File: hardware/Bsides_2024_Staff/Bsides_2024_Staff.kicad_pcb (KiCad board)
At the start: 2 copper layers, 129.4 x 129.4 mm, 59 parts, among them J1 Serial_IN, J2 Add_On, J3 OLED, J4 Serial_OUT, J5 Battery, J6 Battery, P1 USB_C_Plug_USB2.0, Q1 DMG3415U-7, SW1 ON, SW2 RESET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

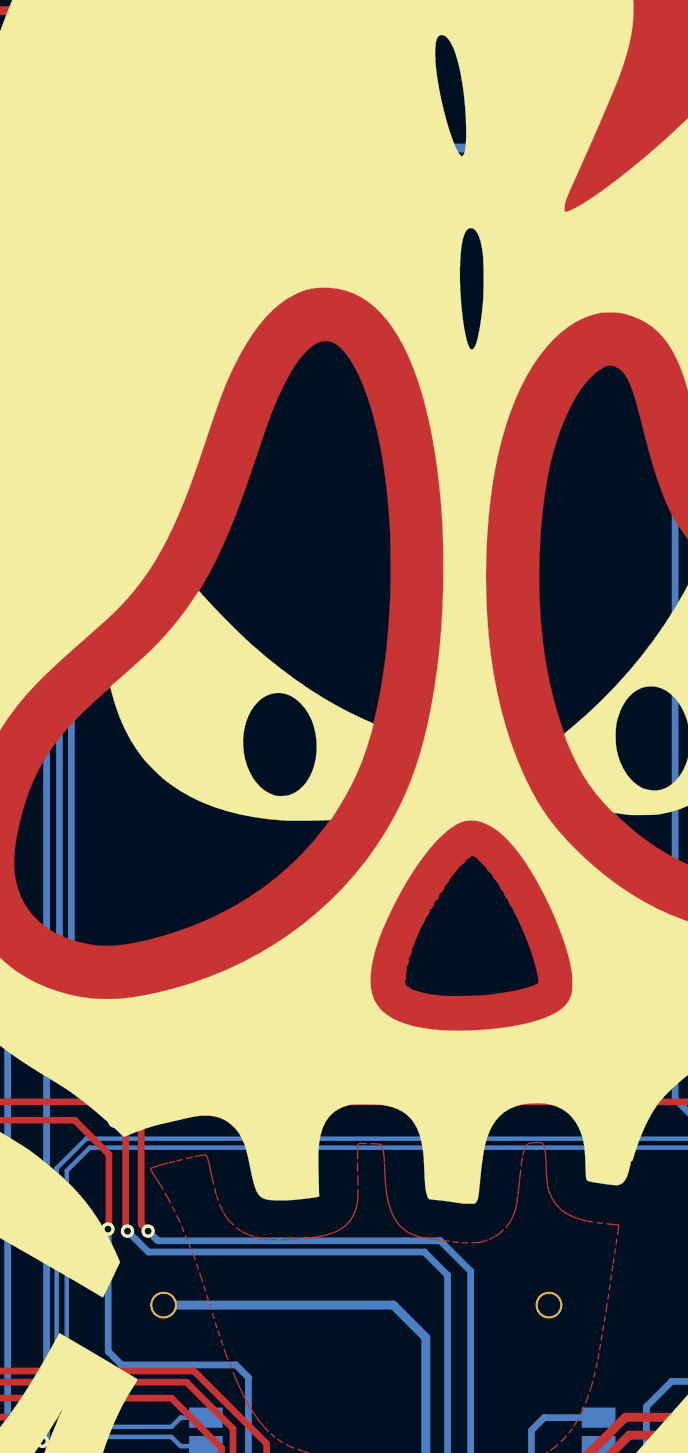
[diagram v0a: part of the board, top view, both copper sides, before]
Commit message: feat(Hw):Update_Labels_SCH_PCB_Sponsor_And_Staff
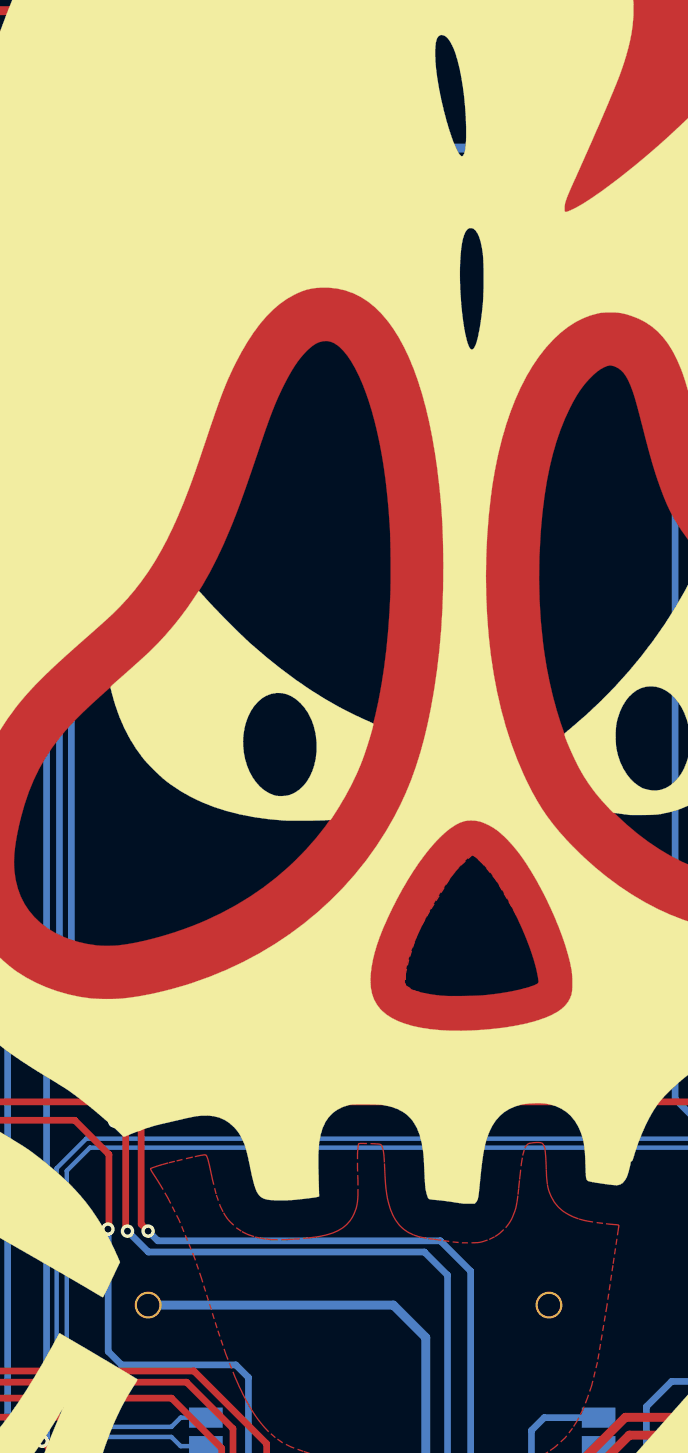
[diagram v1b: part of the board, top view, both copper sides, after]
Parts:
- added kibuzzard-666C8913: G***, kibuzzard-666C8913, B.Cu at (169.5, 130.3)
- added kibuzzard-666C8921: G***, kibuzzard-666C8921, B.Cu at (166.5, 140.2)
- added kibuzzard-666C8949: G***, kibuzzard-666C8949, B.Cu at (196.4, 132.0)
- added kibuzzard-666C8959: G***, kibuzzard-666C8959, B.Cu at (126.1, 131.6)
- added kibuzzard-666C89E6: G***, kibuzzard-666C89E6, B.Cu at (120.3, 86.3)
- added kibuzzard-666C89FF: G***, kibuzzard-666C89FF, B.Cu at (123.3, 74.8)
- moved J5 0.69 mm to (139.1, 100.3)
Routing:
- net Net-(J5-Pin_1): track 17.2 -> 17.9 mm
- net +BATT: track 59.7 -> 60.4 mm

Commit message: feat(hw): add logos staff
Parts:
- removed kibuzzard-666B5C24: G***, kibuzzard-666B5C24
- removed kibuzzard-666B5C33: G***, kibuzzard-666B5C33
- added G***: LOGO, LOGO, B.Cu at (150.4, 42.3)
- added G***: LOGO, LOGO, B.Cu at (168.9, 54.9)
- added REF**: OSHW-Logo_7.5x8mm_SilkScreen, Symbol:OSHW-Logo_7.5x8mm_SilkScreen, B.Cu at (129.5, 46.7)
- added kibuzzard-666C8E87: G***, kibuzzard-666C8E87, B.Cu at (151.7, 37.2)
- added kibuzzard-666C9266: G***, kibuzzard-666C9266, B.Cu at (136.5, 60.2)
- added kibuzzard-666C926F: G***, kibuzzard-666C926F, B.Cu at (136.4, 68.8)
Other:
- board text added: "4e6576657220676f6e6e612067 69766520796f752075700a4e65 76657220676f6e6e61206c6574 20796f7520646f776e0a4e6576 657220676f6e6e612072756e20 61726f756e6420616e64206465 7365727420796f75"
- board text added: "Aqui inicia el tour por latinoamerica Parce Wey Che"
- board text added: "Elige tu bando, rudo o tecnico?"
- board text added: "Lucharan de 2 a 3 caidas sin limite de tiempo!!"

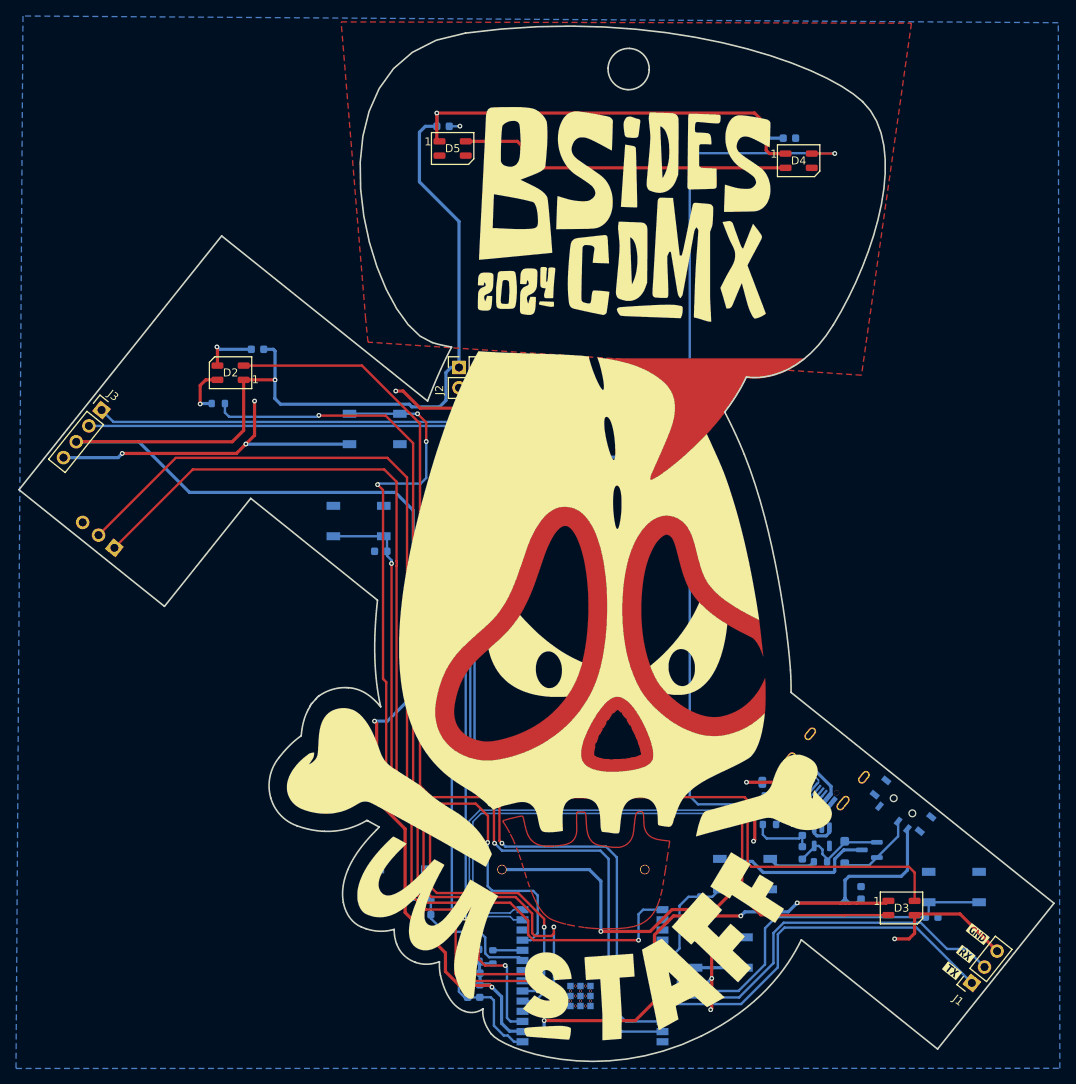
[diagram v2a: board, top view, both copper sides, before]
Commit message: feat(Hw):Update_footprint_badge
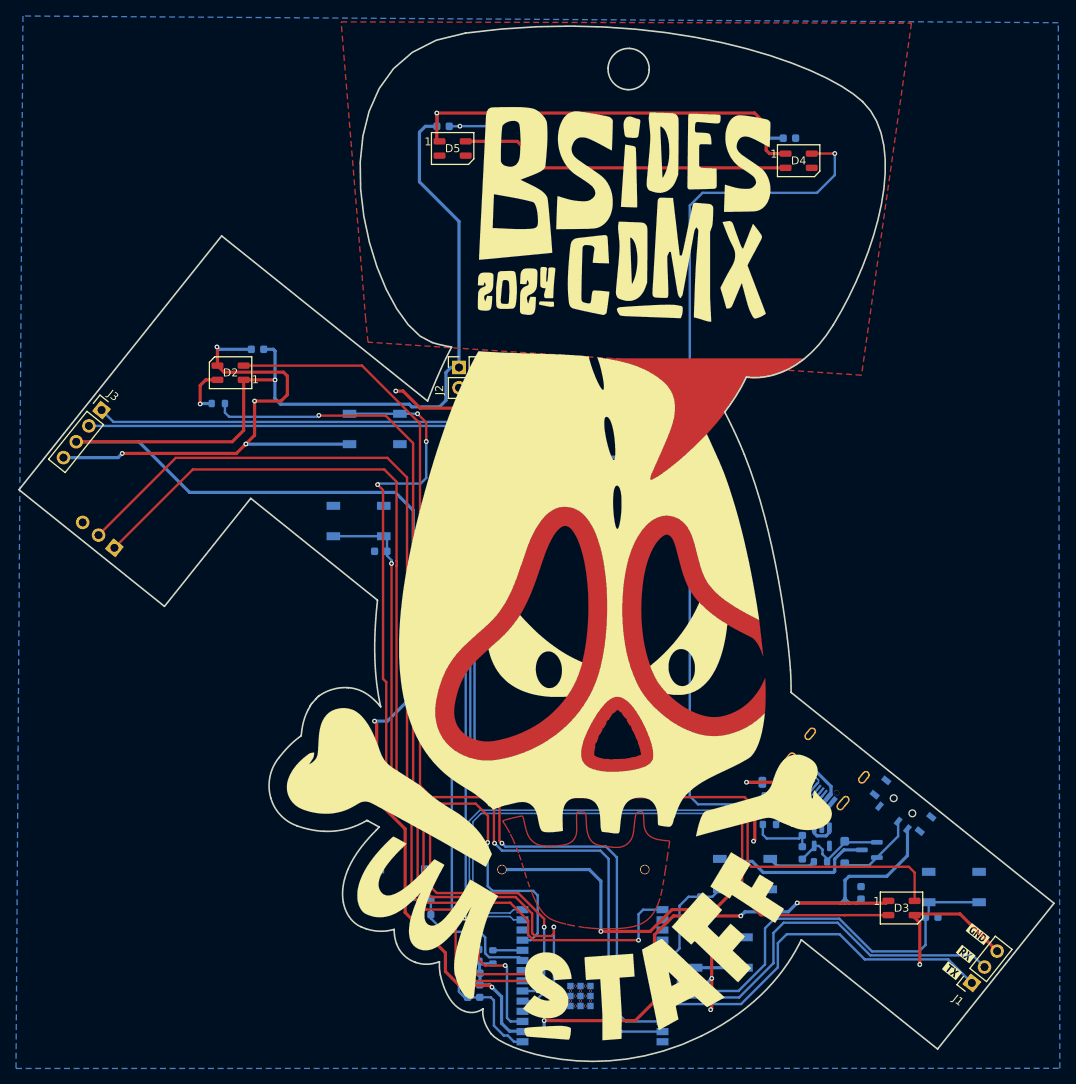
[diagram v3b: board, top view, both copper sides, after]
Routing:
- net GND: track 137.3 -> 163.4 mm, vias 13 -> 14
- net /RIGHT: track 47.7 -> 53.1 mm
- net Net-(D3-DOUT): track 138.6 -> 136.9 mm
- net /TX: track 48.3 -> 47.0 mm
- net /VOUT: track 372.6 -> 371.6 mm

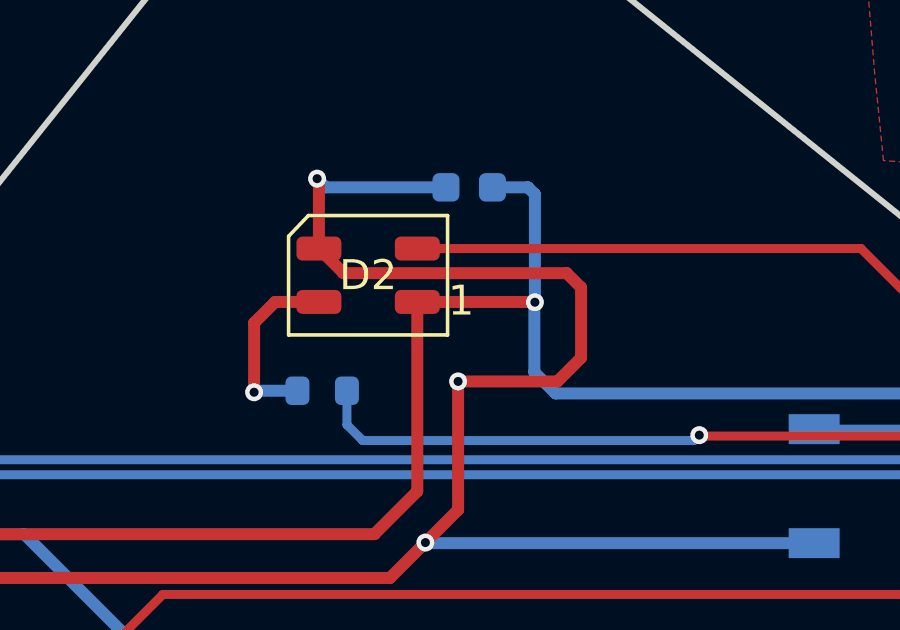
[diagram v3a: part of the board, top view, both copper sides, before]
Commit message: feat(Hw): Update labels
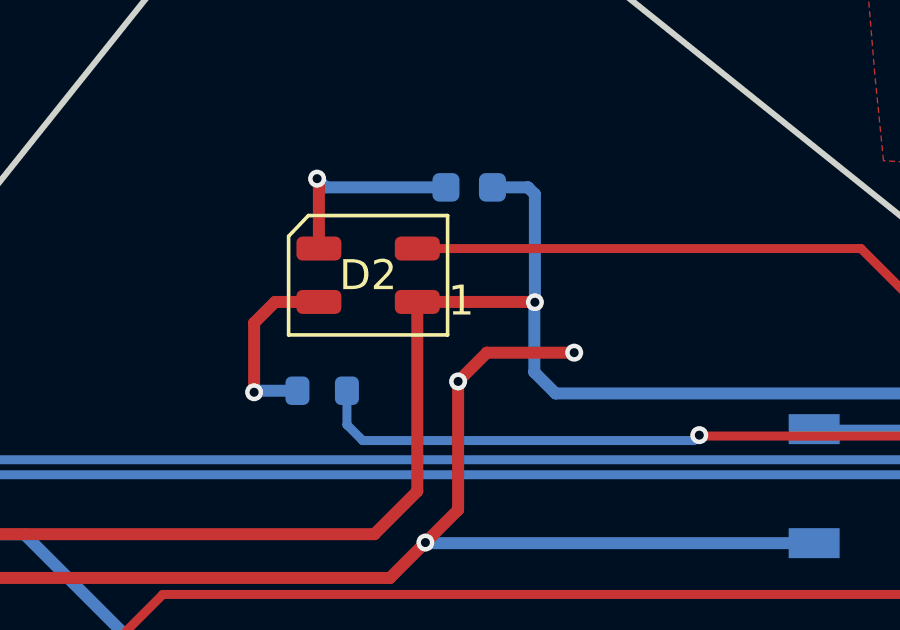
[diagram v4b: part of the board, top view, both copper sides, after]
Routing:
- net GND: track 163.4 -> 151.6 mm, vias 14 -> 15
